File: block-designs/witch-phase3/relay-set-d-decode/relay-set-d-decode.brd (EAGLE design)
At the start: 98.8 x 75.2 mm, 67 parts, among them IC1 74LS138D, IC10 74LVC1G125DBV, IC11 74LVC1G125DBV, IC12 74LVC1G125DBV, IC13 74LVC1G125DBV, IC14 74LVC1G125DBV, IC2 74LS138D, IC3 74LS138D, IC4 74LS138D, IC5 74LVC1G125DBV, IC6 74LVC1G125DBV, IC7 74LVC1G125DBV, IC8 74LVC1G125DBV, IC9 74LVC1G125DBV

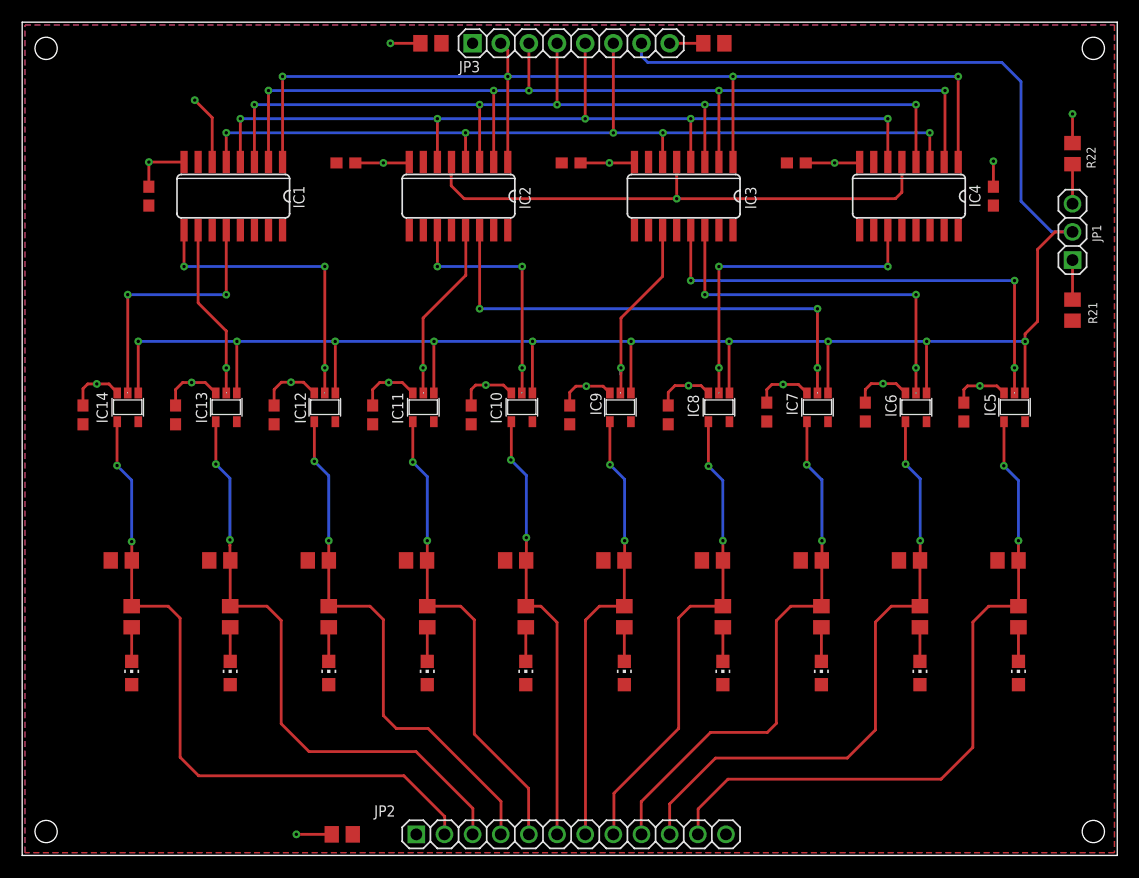
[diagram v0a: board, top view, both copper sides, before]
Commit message: updated layout to center connectors
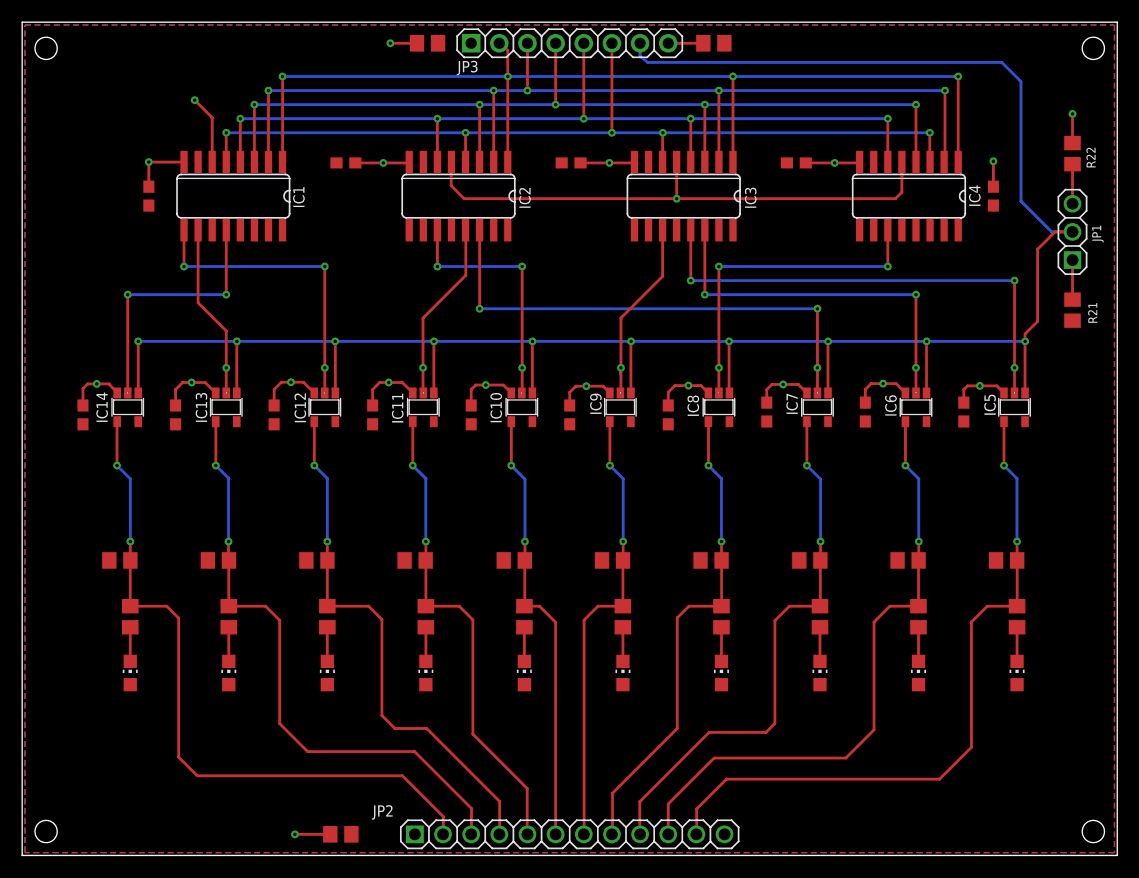
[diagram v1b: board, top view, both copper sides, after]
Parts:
- moved C5 0.30 mm to (36.6, 73.3)
- moved LED1 0.13 mm to (89.8, 16.5)
- moved LED2 0.13 mm to (80.9, 16.5)
- moved LED3 0.13 mm to (72.0, 16.5)
- moved R11 0.13 mm to (89.8, 21.5)
- moved R12 0.13 mm to (80.9, 21.5)
- moved R13 0.13 mm to (72.0, 21.5)
- moved R3 0.13 mm to (71.1, 26.6)
- moved JP2 0.13 mm to (49.4, 1.91)
- moved JP3 0.13 mm to (49.4, 73.3)
- moved LED6 0.13 mm to (45.3, 16.5)
- moved LED7 0.13 mm to (36.4, 16.5)
- moved LED9 0.13 mm to (18.6, 16.5)
- moved R16 0.13 mm to (45.3, 21.5)
- moved R17 0.13 mm to (36.4, 21.5)
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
